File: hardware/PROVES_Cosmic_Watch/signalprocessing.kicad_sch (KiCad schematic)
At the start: 18 parts, among them J3 Conn_Coaxial, U4 LT1807

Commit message: Updates
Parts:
- C3, R6: footprint (none) -> RC0805JR-070RL:R0805
- D1, D2: footprint (none) -> OnSemi MBR0540:SOD-123_L2.8-W1.8-LS3.7-RD
- U3: renamed from U4; footprint (none) -> LT1807MSOP:MSOP-8_MS_LIT
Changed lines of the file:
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@@
 			)
 		)
-		(property "Footprint" ""
+		(property "Footprint" "RC0805JR-070RL:R0805"
 			(at 217.17 88.9 0)
 			(effects
@@
 		(dnp no)
 		(fields_autoplaced yes)
-		(property "Reference" "U4"
+		(property "Reference" "U3"
 			(at 116.84 76.2 0)
 			(effects
@@
 			)
 		)
-		(property "Footprint" ""
+		(property "Footprint" "LT1807MSOP:MSOP-8_MS_LIT"
 			(at 116.84 86.36 0)
 			(effects
@@
 			(project "Cosmic_Watch"
 				(path "/901a4a81-3d4a-4d59-b0fc-ea1dade1210f/7e234915-02ab-46f1-97e9-144c63994663"
-					(reference "U4")
+					(reference "U3")
 					(unit 1)
 				)
@@
 		(dnp no)
 		(fields_autoplaced yes)
-		(property "Reference" "U4"
+		(property "Reference" "U3"
 			(at 162.56 78.74 0)
 			(effects
@@
 			)
 		)
-		(property "Footprint" ""
+		(property "Footprint" "LT1807MSOP:MSOP-8_MS_LIT"
 			(at 162.56 88.9 0)
 			(effects
@@
 			(project "Cosmic_Watch"
 				(path "/901a4a81-3d4a-4d59-b0fc-ea1dade1210f/7e234915-02ab-46f1-97e9-144c63994663"
-					(reference "U4")
+					(reference "U3")
 					(unit 2)
 				)
@@
 			)
 		)
-		(property "Footprint" ""
+		(property "Footprint" "RC0805JR-070RL:R0805"
 			(at 231.14 88.9 0)
 			(effects
@@
 			)
 		)
-		(property "Footprint" ""
+		(property "Footprint" "OnSemi MBR0540:SOD-123_L2.8-W1.8-LS3.7-RD"
 			(at 166.37 100.33 0)
 			(effects
@@
 			)
 		)
-		(property "Footprint" ""
+		(property "Footprint" "OnSemi MBR0540:SOD-123_L2.8-W1.8-LS3.7-RD"
 			(at 185.42 88.9 0)
 			(effects
@@
 		(dnp no)
 		(fields_autoplaced yes)
-		(property "Reference" "U4"
+		(property "Reference" "U3"
 			(at 34.29 86.3599 0)
 			(effects
@@
 			)
 		)
-		(property "Footprint" ""
+		(property "Footprint" "LT1807MSOP:MSOP-8_MS_LIT"
 			(at 35.56 87.63 0)
 			(effects
@@
 			(project "Cosmic_Watch"
 				(path "/901a4a81-3d4a-4d59-b0fc-ea1dade1210f/7e234915-02ab-46f1-97e9-144c63994663"
-					(reference "U4")
+					(reference "U3")
 					(unit 3)
 				)

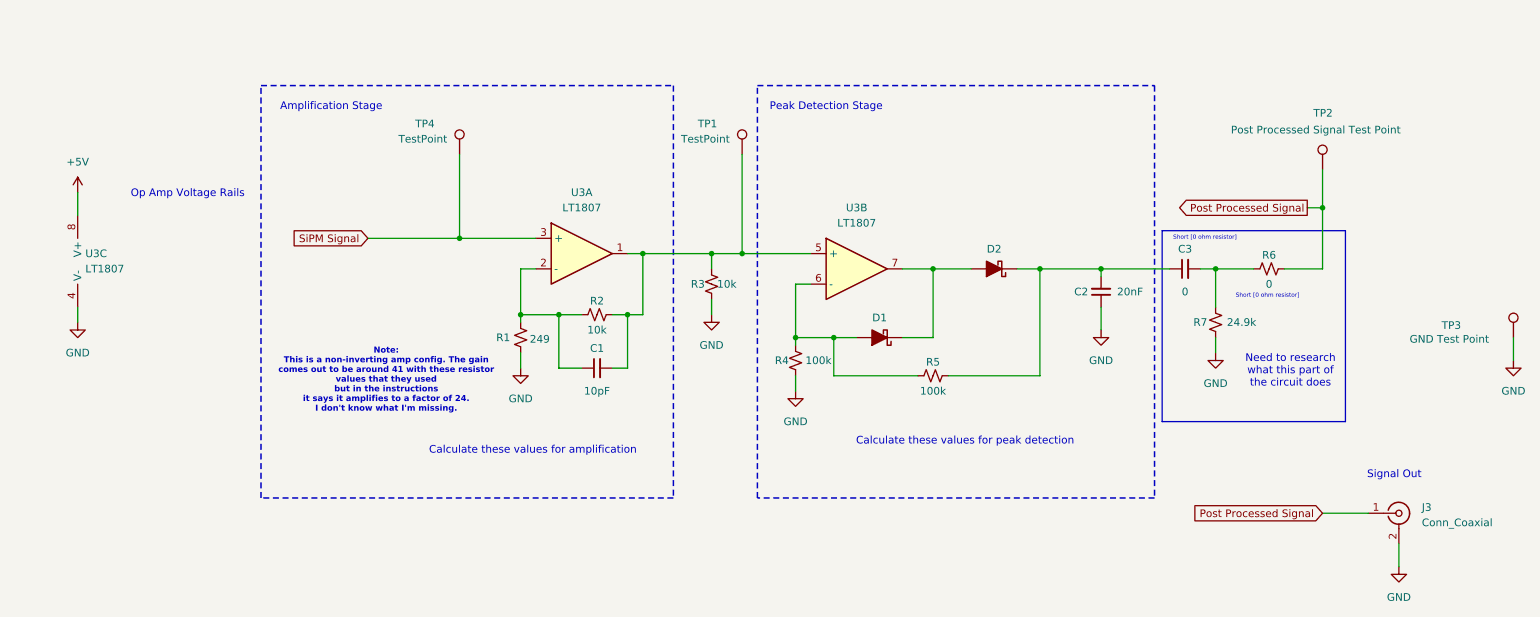
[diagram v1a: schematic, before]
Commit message: Added Footprints and Started Layout
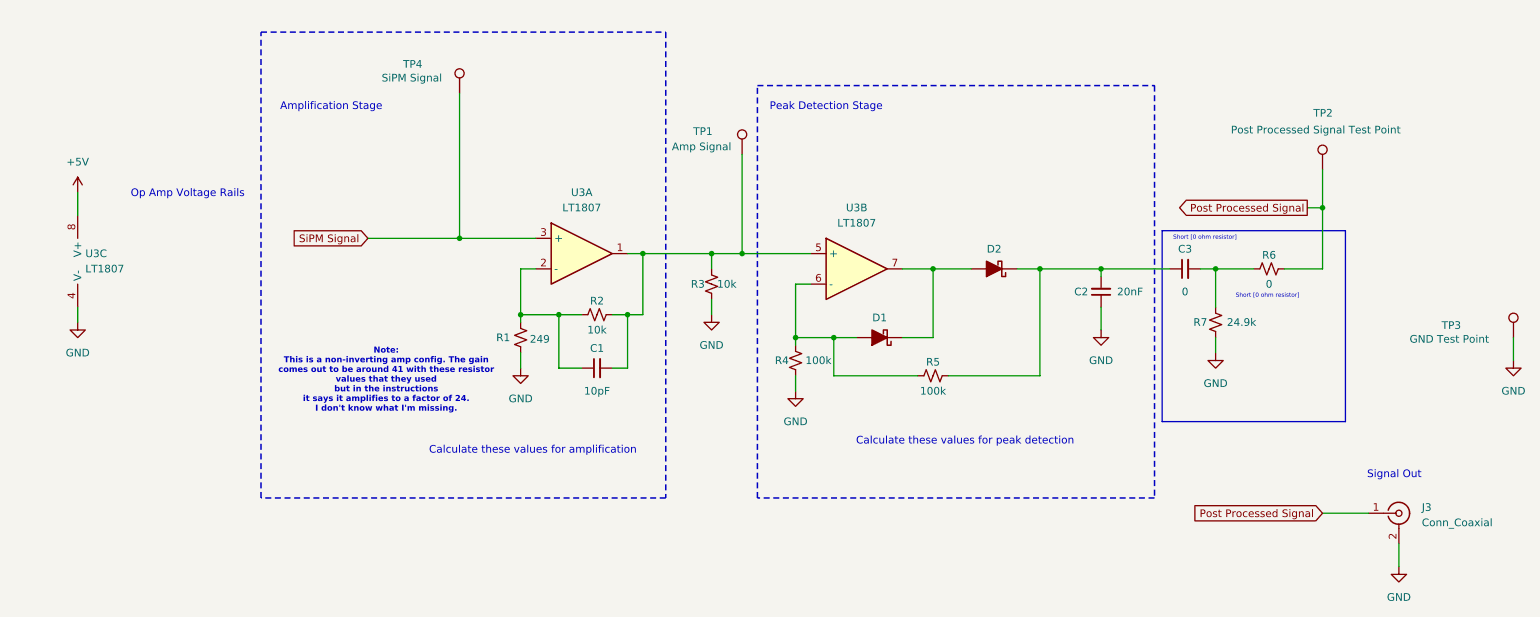
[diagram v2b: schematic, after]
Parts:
- C1, C2: footprint (none) -> Capacitor_SMD:C_0805_2012Metric
- J3: footprint (none) -> Connector_Coaxial:SMA_Amphenol_901-144_Vertical
- R1, R2, R3, R4, R5, R7: footprint (none) -> Resistor_SMD:R_0805_2012Metric
- TP1: value TestPoint -> Amp Signal; footprint (none) -> TestPoint:TestPoint_Keystone_5000-5004_Miniature
- TP2, TP3: footprint (none) -> TestPoint:TestPoint_Keystone_5000-5004_Miniature
- TP4: value TestPoint -> SiPM Signal; footprint (none) -> TestPoint:TestPoint_Keystone_5000-5004_Miniature
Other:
- note removed: "Need to research what this part of the circuit does"
- moved on the sheet: TP4
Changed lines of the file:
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@@
 	(paper "A4")
 	(rectangle
-		(start 63.5 58.42)
-		(end 132.08 127)
+		(start 63.5 49.53)
+		(end 130.81 127)
 		(stroke
 			(width 0.25)
@@
 		(exclude_from_sim no)
 		(at 108.712 119.126 0)
-		(effects
-			(font
-				(size 1.27 1.27)
-			)
-		)
-	)
-	(text "Need to research \nwhat this part of \nthe circuit does"
-		(exclude_from_sim no)
-		(at 234.696 105.918 0)
 		(effects
 			(font
@@
 	)
 	(junction
+		(at 96.52 83.82)
+		(diameter 0)
+		(color 0 0 0 0)
+	)
+	(junction
 		(at 106.68 96.52)
 		(diameter 0)
@@
 	)
 	(junction
-		(at 96.52 83.82)
-		(diameter 0)
-		(color 0 0 0 0)
-	)
-	(junction
 		(at 143.51 86.36)
 		(diameter 0)
@@
 	(wire
 		(pts
+			(xy 96.52 59.69) (xy 96.52 83.82)
+		)
+		(stroke
+			(width 0)
+			(type default)
+		)
+	)
+	(wire
+		(pts
 			(xy 233.68 88.9) (xy 240.03 88.9)
 		)
@@
 	(wire
 		(pts
-			(xy 96.52 69.85) (xy 96.52 83.82)
-		)
-		(stroke
-			(width 0)
-			(type default)
-		)
-	)
-	(wire
-		(pts
 			(xy 152.4 91.44) (xy 152.4 100.33)
 		)
@@
 	(wire
 		(pts
+			(xy 143.51 69.85) (xy 143.51 86.36)
+		)
+		(stroke
+			(width 0)
+			(type default)
+		)
+	)
+	(wire
+		(pts
+			(xy 175.26 88.9) (xy 181.61 88.9)
+		)
+		(stroke
+			(width 0)
+			(type default)
+		)
+	)
+	(wire
+		(pts
+			(xy 158.75 106.68) (xy 158.75 100.33)
+		)
+		(stroke
+			(width 0)
+			(type default)
+		)
+	)
+	(wire
+		(pts
+			(xy 152.4 100.33) (xy 158.75 100.33)
+		)
+		(stroke
+			(width 0)
+			(type default)
+		)
+	)
+	(wire
+		(pts
+			(xy 124.46 96.52) (xy 127 96.52)
+		)
+		(stroke
+			(width 0)
+			(type default)
+		)
+	)
+	(wire
+		(pts
+			(xy 170.18 100.33) (xy 175.26 100.33)
+		)
+		(stroke
+			(width 0)
+			(type default)
+		)
+	)
+	(wire
+		(pts
+			(xy 203.2 95.25) (xy 203.2 99.06)
+		)
+		(stroke
+			(width 0)
+			(type default)
+		)
+	)
+	(wire
+		(pts
+			(xy 193.04 88.9) (xy 193.04 106.68)
+		)
+		(stroke
+			(width 0)
+			(type default)
+		)
+	)
+	(wire
+		(pts
+			(xy 106.68 96.52) (xy 106.68 97.79)
+		)
+		(stroke
+			(width 0)
+			(type default)
+		)
+	)
+	(wire
+		(pts
+			(xy 106.68 88.9) (xy 106.68 96.52)
+		)
+		(stroke
+			(width 0)
+			(type default)
+		)
+	)
+	(wire
+		(pts
+			(xy 124.46 105.41) (xy 124.46 96.52)
+		)
+		(stroke
+			(width 0)
+			(type default)
+		)
+	)
+	(wire
+		(pts
+			(xy 189.23 88.9) (xy 193.04 88.9)
+		)
+		(stroke
+			(width 0)
+			(type default)
+		)
+	)
+	(wire
+		(pts
+			(xy 240.03 72.39) (xy 240.03 78.74)
+		)
+		(stroke
+			(width 0)
+			(type default)
+		)
+	)
+	(wire
+		(pts
 			(xy 96.52 83.82) (xy 109.22 83.82)
-		)
-		(stroke
-			(width 0)
-			(type default)
-		)
-	)
-	(wire
-		(pts
-			(xy 143.51 69.85) (xy 143.51 86.36)
-		)
-		(stroke
-			(width 0)
-			(type default)
-		)
-	)
-	(wire
-		(pts
-			(xy 175.26 88.9) (xy 181.61 88.9)
-		)
-		(stroke
-			(width 0)
-			(type default)
-		)
-	)
-	(wire
-		(pts
-			(xy 158.75 106.68) (xy 158.75 100.33)
-		)
-		(stroke
-			(width 0)
-			(type default)
-		)
-	)
-	(wire
-		(pts
-			(xy 152.4 100.33) (xy 158.75 100.33)
-		)
-		(stroke
-			(width 0)
-			(type default)
-		)
-	)
-	(wire
-		(pts
-			(xy 124.46 96.52) (xy 127 96.52)
-		)
-		(stroke
-			(width 0)
-			(type default)
-		)
-	)
-	(wire
-		(pts
-			(xy 170.18 100.33) (xy 175.26 100.33)
-		)
-		(stroke
-			(width 0)
-			(type default)
-		)
-	)
-	(wire
-		(pts
-			(xy 203.2 95.25) (xy 203.2 99.06)
-		)
-		(stroke
-			(width 0)
-			(type default)
-		)
-	)
-	(wire
-		(pts
-			(xy 193.04 88.9) (xy 193.04 106.68)
-		)
-		(stroke
-			(width 0)
-			(type default)
-		)
-	)
-	(wire
-		(pts
-			(xy 106.68 96.52) (xy 106.68 97.79)
-		)
-		(stroke
-			(width 0)
-			(type default)
-		)
-	)
-	(wire
-		(pts
-			(xy 106.68 88.9) (xy 106.68 96.52)
-		)
-		(stroke
-			(width 0)
-			(type default)
-		)
-	)
-	(wire
-		(pts
-			(xy 124.46 105.41) (xy 124.46 96.52)
-		)
-		(stroke
-			(width 0)
-			(type default)
-		)
-	)
-	(wire
-		(pts
-			(xy 189.23 88.9) (xy 193.04 88.9)
-		)
-		(stroke
-			(width 0)
-			(type default)
-		)
-	)
-	(wire
-		(pts
-			(xy 240.03 72.39) (xy 240.03 78.74)
 		)
 		(stroke
@@
 			)
 		)
-		(property "Footprint" ""
+		(property "Footprint" "Capacitor_SMD:C_0805_2012Metric"
 			(at 119.38 105.41 0)
 			(effects
@@
 			)
 		)
-		(property "Footprint" ""
+		(property "Footprint" "TestPoint:TestPoint_Keystone_5000-5004_Miniature"
 			(at 245.11 72.39 0)
 			(effects
@@
 			)
 		)
-		(property "Footprint" ""
+		(property "Footprint" "Resistor_SMD:R_0805_2012Metric"
 			(at 119.38 96.52 0)
 			(effects
@@
 			)
 		)
-		(property "Footprint" ""
+		(property "Footprint" "Resistor_SMD:R_0805_2012Metric"
 			(at 222.25 97.79 0)
 			(effects
@@
 	(symbol
 		(lib_id "Connector:TestPoint")
-		(at 96.52 69.85 0)
+		(at 96.52 59.69 0)
 		(unit 1)
 		(exclude_from_sim no)
@@
 		(dnp no)
 		(property "Reference" "TP4"
-			(at 89.154 64.77 0)
+			(at 87.122 54.864 0)
 			(effects
 				(font
@@
 			)
 		)
-		(property "Value" "TestPoint"
-			(at 86.36 67.31 0)
+		(property "Value" "SiPM Signal"
+			(at 83.566 57.15 0)
 			(effects
 				(font
@@
 			)
 		)
-		(property "Footprint" ""
-			(at 101.6 69.85 0)
+		(property "Footprint" "TestPoint:TestPoint_Keystone_5000-5004_Miniature"
+			(at 101.6 59.69 0)
 			(effects
 				(font
@@
 		)
 		(property "Datasheet" "~"
-			(at 101.6 69.85 0)
+			(at 101.6 59.69 0)
 			(effects
 				(font
@@
 		)
 		(property "Description" "test point"
-			(at 96.52 69.85 0)
+			(at 96.52 59.69 0)
 			(effects
 				(font
@@
 			)
 		)
-		(property "Footprint" ""
+		(property "Footprint" "Connector_Coaxial:SMA_Amphenol_901-144_Vertical"
 			(at 252.73 129.54 0)
 			(effects
@@
 			)
 		)
-		(property "Footprint" ""
+		(property "Footprint" "Resistor_SMD:R_0805_2012Metric"
 			(at 175.26 106.68 0)
 			(effects
@@
 			)
 		)
-		(property "Footprint" ""
+		(property "Footprint" "Capacitor_SMD:C_0805_2012Metric"
 			(at 203.2 92.71 0)
 			(effects
@@
 			)
 		)
-		(property "Footprint" ""
+		(property "Footprint" "Resistor_SMD:R_0805_2012Metric"
 			(at 152.4 104.14 0)
 			(effects
@@
 		(dnp no)
 		(property "Reference" "TP1"
-			(at 136.144 64.77 0)
+			(at 135.382 66.04 0)
 			(effects
 				(font
@@
 			)
 		)
-		(property "Value" "TestPoint"
-			(at 133.35 67.31 0)
+		(property "Value" "Amp Signal"
+			(at 131.826 68.58 0)
 			(effects
 				(font
@@
 			)
 		)
-		(property "Footprint" ""
+		(property "Footprint" "TestPoint:TestPoint_Keystone_5000-5004_Miniature"
 			(at 148.59 69.85 0)
 			(effects
@@
 			)
 		)
-		(property "Footprint" ""
+		(property "Footprint" "Resistor_SMD:R_0805_2012Metric"
 			(at 106.68 100.33 0)
 			(effects
@@
 			)
 		)
-		(property "Footprint" ""
+		(property "Footprint" "Resistor_SMD:R_0805_2012Metric"
 			(at 138.43 91.44 0)
 			(effects
@@
 			)
 		)
-		(property "Footprint" ""
+		(property "Footprint" "TestPoint:TestPoint_Keystone_5000-5004_Miniature"
 			(at 276.86 100.33 0)
 			(effects

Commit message: Layout Updates
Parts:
- added C4: 10uF, Capacitor_SMD:C_0805_2012Metric_Pad1.18x1.45mm_HandSolder, symbol Device:C_Small
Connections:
- net +5V: now also C4.1
- net GND: now also C4.2
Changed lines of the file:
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@@
 	(text "Op Amp Voltage Rails"
 		(exclude_from_sim no)
-		(at 51.308 76.454 0)
+		(at 52.07 47.752 0)
 		(effects
 			(font
@@
 	)
 	(junction
+		(at 33.02 77.47)
+		(diameter 0)
+		(color 0 0 0 0)
+	)
+	(junction
 		(at 106.68 96.52)
 		(diameter 0)
@@
 	(wire
 		(pts
-			(xy 33.02 76.2) (xy 33.02 80.01)
+			(xy 33.02 76.2) (xy 33.02 77.47)
 		)
 		(stroke
@@
 	(wire
 		(pts
+			(xy 33.02 77.47) (xy 41.91 77.47)
+		)
+		(stroke
+			(width 0)
+			(type default)
+		)
+	)
+	(wire
+		(pts
 			(xy 152.4 91.44) (xy 152.4 100.33)
 		)
@@
 	(wire
 		(pts
+			(xy 33.02 77.47) (xy 33.02 80.01)
+		)
+		(stroke
+			(width 0)
+			(type default)
+		)
+	)
+	(wire
+		(pts
 			(xy 124.46 86.36) (xy 127 86.36)
 		)
@@
 		(pts
 			(xy 203.2 88.9) (xy 214.63 88.9)
+		)
+		(stroke
+			(width 0)
+			(type default)
+		)
+	)
+	(wire
+		(pts
+			(xy 41.91 85.09) (xy 41.91 82.55)
 		)
 		(stroke
@@
 	)
 	(symbol
+		(lib_id "power:GND")
+		(at 41.91 85.09 0)
+		(unit 1)
+		(exclude_from_sim no)
+		(in_bom yes)
+		(on_board yes)
+		(dnp no)
+		(fields_autoplaced yes)
+		(property "Reference" "#PWR011"
+			(at 41.91 91.44 0)
+			(effects
+				(font
+					(size 1.27 1.27)
+				)
+				(hide yes)
+			)
+		)
+		(property "Value" "GND"
+			(at 41.91 90.17 0)
+			(effects
+				(font
+					(size 1.27 1.27)
+				)
+			)
+		)
+		(property "Footprint" ""
+			(at 41.91 85.09 0)
+			(effects
+				(font
+					(size 1.27 1.27)
+				)
+				(hide yes)
+			)
+		)
+		(property "Datasheet" ""
+			(at 41.91 85.09 0)
+			(effects
+				(font
+					(size 1.27 1.27)
+				)
+				(hide yes)
+			)
+		)
+		(property "Description" "Power symbol creates a global label with name \"GND\" , ground"
+			(at 41.91 85.09 0)
+			(effects
+				(font
+					(size 1.27 1.27)
+				)
+				(hide yes)
+			)
+		)
+		(pin "1"
+		)
+		(instances
+			(project "PROVES_Cosmic_Watch"
+				(path "/901a4a81-3d4a-4d59-b0fc-ea1dade1210f/7e234915-02ab-46f1-97e9-144c63994663"
+					(reference "#PWR011")
+					(unit 1)
+				)
+			)
+		)
+	)
+	(symbol
 		(lib_id "Device:R_Small_US")
 		(at 119.38 96.52 90)
@@
 	)
 	(symbol
+		(lib_id "Device:C_Small")
+		(at 41.91 80.01 0)
+		(unit 1)
+		(exclude_from_sim no)
+		(in_bom yes)
+		(on_board yes)
+		(dnp no)
+		(fields_autoplaced yes)
+		(property "Reference" "C4"
+			(at 44.45 78.7462 0)
+			(effects
+				(font
+					(size 1.27 1.27)
+				)
+				(justify left)
+			)
+		)
+		(property "Value" "10uF"
+			(at 44.45 81.2862 0)
+			(effects
+				(font
+					(size 1.27 1.27)
+				)
+				(justify left)
+			)
+		)
+		(property "Footprint" "Capacitor_SMD:C_0805_2012Metric_Pad1.18x1.45mm_HandSolder"
+			(at 41.91 80.01 0)
+			(effects
+				(font
+					(size 1.27 1.27)
+				)
+				(hide yes)
+			)
+		)
+		(property "Datasheet" "~"
+			(at 41.91 80.01 0)
+			(effects
+				(font
+					(size 1.27 1.27)
+				)
+				(hide yes)
+			)
+		)
+		(property "Description" "Unpolarized capacitor, small symbol"
+			(at 41.91 80.01 0)
+			(effects
+				(font
+					(size 1.27 1.27)
+				)
+				(hide yes)
+			)
+		)
+		(pin "2"
+		)
+		(pin "1"
+		)
+		(instances
+			(project ""
+				(path "/901a4a81-3d4a-4d59-b0fc-ea1dade1210f/7e234915-02ab-46f1-97e9-144c63994663"
+					(reference "C4")
+					(unit 1)
+				)
+			)
+		)
+	)
+	(symbol
 		(lib_id "power:GND")
 		(at 33.02 97.79 0)
@@
 		(on_board yes)
 		(dnp no)
-		(fields_autoplaced yes)
 		(property "Reference" "U3"
-			(at 34.29 86.3599 0)
+			(at 22.098 85.852 0)
 			(effects
 				(font
@@
 		)
 		(property "Value" "LT1807"
-			(at 34.29 88.8999 0)
-			(effects
-				(font
+			(at 22.098 88.392 0)
+			(effects
+				(font

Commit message: Layout Updates
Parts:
- added C7: 0.1uF, Capacitor_SMD:C_0805_2012Metric, symbol Device:C_Small
- C4: footprint Capacitor_SMD:C_0805_2012Metric_Pad1.18x1.45mm_HandSolder -> Capacitor_SMD:C_0805_2012Metric
- TP2: value Post Processed Signal Test Point -> PPS
- TP3: value GND Test Point -> GND
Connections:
- net +5V: now also C7.1
- net GND: now also C7.2
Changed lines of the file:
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@@
+	)
+	(junction
+		(at 41.91 77.47)
+		(diameter 0)
+		(color 0 0 0 0)
 	)
 	(junction
@@
 	(wire
 		(pts
+			(xy 52.07 82.55) (xy 52.07 85.09)
+		)
+		(stroke
+			(width 0)
+			(type default)
+		)
+	)
+	(wire
+		(pts
 			(xy 240.03 129.54) (xy 247.65 129.54)
 		)
@@
 		(pts
 			(xy 158.75 100.33) (xy 162.56 100.33)
+		)
+		(stroke
+			(width 0)
+			(type default)
+		)
+	)
+	(wire
+		(pts
+			(xy 41.91 77.47) (xy 52.07 77.47)
 		)
 		(stroke
@@
 			)
 		)
-		(property "Value" "Post Processed Signal Test Point"
-			(at 224.79 65.786 0)
+		(property "Value" "PPS"
+			(at 238.506 65.532 0)
 			(effects
 				(font
@@
 				(path "/901a4a81-3d4a-4d59-b0fc-ea1dade1210f/7e234915-02ab-46f1-97e9-144c63994663"
 					(reference "TP2")
+					(unit 1)
+				)
+			)
+		)
+	)
+	(symbol
+		(lib_id "Device:C_Small")
+		(at 52.07 80.01 0)
+		(unit 1)
+		(exclude_from_sim no)
+		(in_bom yes)
+		(on_board yes)
+		(dnp no)
+		(fields_autoplaced yes)
+		(property "Reference" "C7"
+			(at 54.61 78.7462 0)
+			(effects
+				(font
+					(size 1.27 1.27)
+				)
+				(justify left)
+			)
+		)
+		(property "Value" "0.1uF"
+			(at 54.61 81.2862 0)
+			(effects
+				(font
+					(size 1.27 1.27)
+				)
+				(justify left)
+			)
+		)
+		(property "Footprint" "Capacitor_SMD:C_0805_2012Metric"
+			(at 52.07 80.01 0)
+			(effects
+				(font
+					(size 1.27 1.27)
+				)
+				(hide yes)
+			)
+		)
+		(property "Datasheet" "~"
+			(at 52.07 80.01 0)
+			(effects
+				(font
+					(size 1.27 1.27)
+				)
+				(hide yes)
+			)
+		)
+		(property "Description" "Unpolarized capacitor, small symbol"
+			(at 52.07 80.01 0)
+			(effects
+				(font
+					(size 1.27 1.27)
+				)
+				(hide yes)
+			)
+		)
+		(pin "2"
+		)
+		(pin "1"
+		)
+		(instances
+			(project "PROVES_Cosmic_Watch"
+				(path "/901a4a81-3d4a-4d59-b0fc-ea1dade1210f/7e234915-02ab-46f1-97e9-144c63994663"
+					(reference "C7")
 					(unit 1)
 				)
@@
 	)
 	(symbol
+		(lib_id "power:GND")
+		(at 52.07 85.09 0)
+		(unit 1)
+		(exclude_from_sim no)
+		(in_bom yes)
+		(on_board yes)
+		(dnp no)
+		(fields_autoplaced yes)
+		(property "Reference" "#PWR01"
+			(at 52.07 91.44 0)
+			(effects
+				(font
+					(size 1.27 1.27)
+				)
+				(hide yes)
+			)
+		)
+		(property "Value" "GND"
+			(at 52.07 90.17 0)
+			(effects
+				(font
+					(size 1.27 1.27)
+				)
+			)
+		)
+		(property "Footprint" ""
+			(at 52.07 85.09 0)
+			(effects
+				(font
+					(size 1.27 1.27)
+				)
+				(hide yes)
+			)
+		)
+		(property "Datasheet" ""
+			(at 52.07 85.09 0)
+			(effects
+				(font
+					(size 1.27 1.27)
+				)
+				(hide yes)
+			)
+		)
+		(property "Description" "Power symbol creates a global label with name \"GND\" , ground"
+			(at 52.07 85.09 0)
+			(effects
+				(font
+					(size 1.27 1.27)
+				)
+				(hide yes)
+			)
+		)
+		(pin "1"
+		)
+		(instances
+			(project "PROVES_Cosmic_Watch"
+				(path "/901a4a81-3d4a-4d59-b0fc-ea1dade1210f/7e234915-02ab-46f1-97e9-144c63994663"
+					(reference "#PWR01")
+					(unit 1)
+				)
+			)
+		)
+	)
+	(symbol
 		(lib_id "power:+5V")
 		(at 33.02 76.2 0)
@@
 			)
 		)
-		(property "Footprint" "Capacitor_SMD:C_0805_2012Metric_Pad1.18x1.45mm_HandSolder"
+		(property "Footprint" "Capacitor_SMD:C_0805_2012Metric"
 			(at 41.91 80.01 0)
 			(effects
@@
 			)
 		)
-		(property "Value" "GND Test Point"
-			(at 254.508 100.584 0)
-			(effects
-				(font
+		(property "Value" "GND"
+			(at 259.842 100.838 0)
+			(effects
+				(font

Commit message: Layout Updates
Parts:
- TP4: value SiPM Signal -> SiPM
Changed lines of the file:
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@@
 			)
 		)
-		(property "Value" "SiPM Signal"
-			(at 83.566 57.15 0)
+		(property "Value" "SiPM"
+			(at 86.614 57.15 0)
 			(effects
 				(font

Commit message: updated layout footprint and connections for lt1807
-also updated bom
-changed from package with 3 in stock to 10 in stock
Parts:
- U3: footprint LT1807MSOP:MSOP-8_MS_LIT -> lt1807:SOIC-8_L5.0-W4.0-P1.27-LS6.0-BL
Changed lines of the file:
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@@
 			)
 		)
-		(property "Footprint" "LT1807MSOP:MSOP-8_MS_LIT"
+		(property "Footprint" "lt1807:SOIC-8_L5.0-W4.0-P1.27-LS6.0-BL"
 			(at 116.84 86.36 0)
 			(effects
@@
 			)
 		)
-		(property "Footprint" "LT1807MSOP:MSOP-8_MS_LIT"
+		(property "Footprint" "lt1807:SOIC-8_L5.0-W4.0-P1.27-LS6.0-BL"
 			(at 162.56 88.9 0)
 			(effects
@@
 			)
 		)
-		(property "Footprint" "LT1807MSOP:MSOP-8_MS_LIT"
+		(property "Footprint" "lt1807:SOIC-8_L5.0-W4.0-P1.27-LS6.0-BL"
 			(at 35.56 87.63 0)
 			(effects
